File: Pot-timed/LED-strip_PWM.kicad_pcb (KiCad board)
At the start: 2 copper layers, 29.7 x 10 mm, 16 parts, among them IC1 MADW__ATTINY13-MM, P1 CONN_2, P2 CONN_2, T1 AO3400, U1 MCP1804-SOT23-5

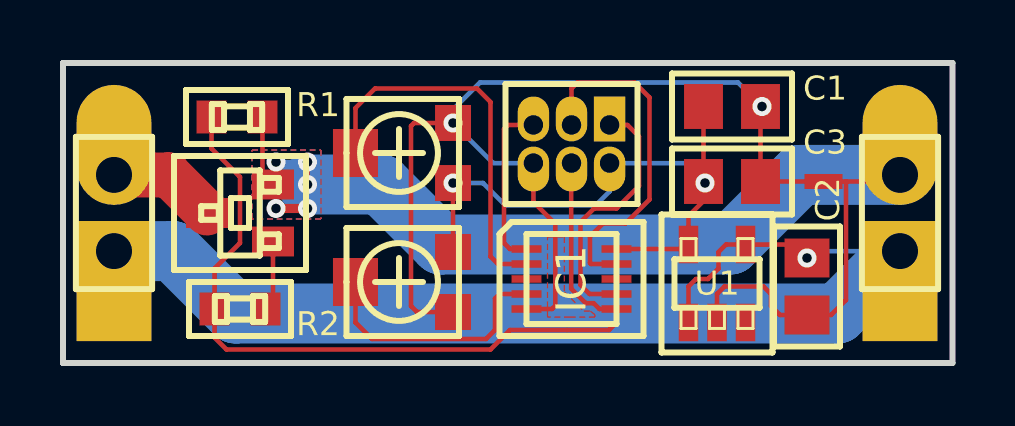
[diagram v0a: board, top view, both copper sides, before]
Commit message: Pot-timed (single board): rounded corners.
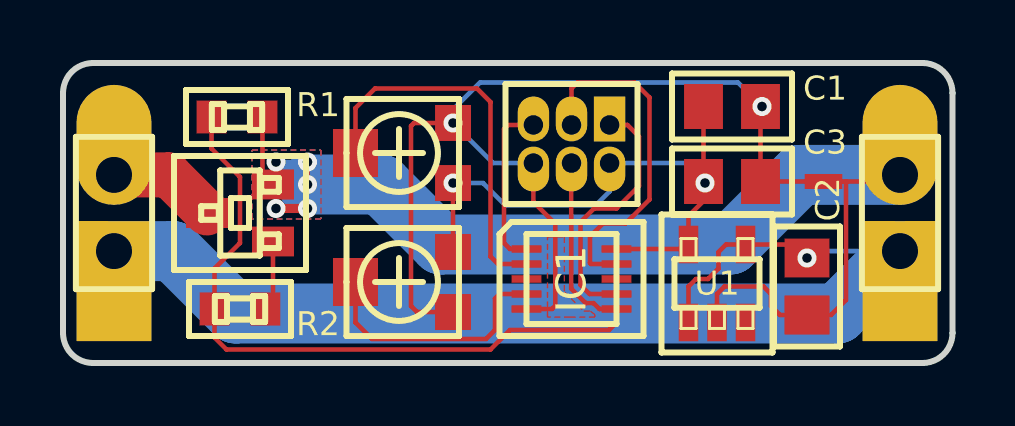
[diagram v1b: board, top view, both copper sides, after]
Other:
- outline, holes or cut-outs redrawn
- board text added: "V0.12 POT PWM controller"
- board text removed: "V0.11 POT PWM controller"
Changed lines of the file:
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@@
-(kicad_pcb (version 3) (host pcbnew "(2013-06-07 BZR 4197)-testing")
+(kicad_pcb (version 3) (host pcbnew "(2013-06-11 BZR 4208)-testing")
   (general
     (links 31)
     (no_connects 0)
-    (area 75.899999 47.899999 105.750001 58.100001)
+    (area 74.5076 46.6476 111.616669 61.100001)
     (thickness 1.6002)
-    (drawings 14)
+    (drawings 18)
     (tracks 156)
     (zones 0)
@@
     (title LED-strip_PWM)
     (date "24 May 2013")
-    (rev 0.11)
+    (rev 0.12)
     (company "2012 - blog.spitzenpfeil.org")
   )
@@
       (xy -0.90932 1.3462)) (layer B.SilkS) (width 0.00254))
   )
+  (gr_line (start 76 57) (end 76 49) (angle 90) (layer Edge.Cuts) (width 0.2))
+  (gr_line (start 104.65 58) (end 77 58) (angle 90) (layer Edge.Cuts) (width 0.2))
+  (gr_line (start 105.65 49) (end 105.65 57) (angle 90) (layer Edge.Cuts) (width 0.2))
+  (gr_line (start 77 48) (end 104.65 48) (angle 90) (layer Edge.Cuts) (width 0.2))
+  (gr_arc (start 104.65 49) (end 104.65 48) (angle 90) (layer Edge.Cuts) (width 0.2))
+  (gr_arc (start 104.65 57) (end 105.65 57) (angle 90) (layer Edge.Cuts) (width 0.2))
+  (gr_arc (start 77 57) (end 77 58) (angle 90) (layer Edge.Cuts) (width 0.2))
+  (gr_arc (start 77 49) (end 76 49) (angle 90) (layer Edge.Cuts) (width 0.2))
   (gr_text + (at 79.7 55.25 90) (layer B.SilkS)
     (effects (font (size 1 1) (thickness 0.2)) (justify mirror))
@@
     (arrow2b (pts (xy 76 59.3) (xy 77.126504 58.713579)))
   )
-  (gr_line (start 105.65 58) (end 76 58) (angle 90) (layer Edge.Cuts) (width 0.2))
-  (gr_line (start 76 48) (end 105.65 48) (angle 90) (layer Edge.Cuts) (width 0.2))
-  (gr_line (start 105.65 58) (end 105.65 48) (angle 90) (layer Edge.Cuts) (width 0.2))
-  (gr_line (start 76 48) (end 76 58) (angle 90) (layer Edge.Cuts) (width 0.2))
-  (gr_text "V0.11\nPOT PWM controller" (at 91 53.2) (layer B.SilkS)
+  (gr_text "V0.12\nPOT PWM controller" (at 91 53.2) (layer B.SilkS)
     (effects (font (size 1 1) (thickness 0.2032)) (justify mirror))
   )
@@
   (segment (start 93.15 48.65) (end 95.05 48.65) (width 0.1524) (layer Front) (net 6))
   (segment (start 92.95 48.85) (end 93.15 48.65) (width 0.1524) (layer Front) (net 6))
+  (segment (start 79.67 54.27) (end 81.75 56.35) (width 2) (layer Back) (net 7))
+  (segment (start 77.7 54.27) (end 79.67 54.27) (width 2) (layer Back) (net 7) (status 10))
+  (segment (start 103.9 54.27) (end 101.82 56.35) (width 2) (layer Back) (net 7) (status 20))
+  (segment (start 81.75 56.35) (end 101.82 56.35) (width 2) (layer Back) (net 7))
   (segment (start 96.85004 56.64794) (end 96.85004 55.44996) (width 0.1524) (layer Front) (net 7) (status 10))
   (segment (start 96.85004 55.44996) (end 97.1 55.2) (width 0.1524) (layer Front) (net 7))
@@
   (segment (start 97.85 54.3) (end 98.1 54.05) (width 0.1524) (layer Front) (net 7))
   (segment (start 98.1 54.05) (end 98.75 54.05) (width 0.1524) (layer Front) (net 7) (status 20))
-  (segment (start 77.7 54.27) (end 79.67 54.27) (width 2) (layer Back) (net 7) (status 10))
-  (segment (start 101.82 56.35) (end 103.9 54.27) (width 2) (layer Back) (net 7) (status 20))
-  (segment (start 81.75 56.35) (end 101.82 56.35) (width 2) (layer Back) (net 7))
-  (segment (start 79.67 54.27) (end 81.75 56.35) (width 2) (layer Back) (net 7))
   (via (at 100.8 54.50004) (size 0.635) (layers Front Back) (net 7) (status 30))
   (segment (start 100.8 54.50004) (end 101.03004 54.27) (width 0.1524) (layer Back) (net 7))

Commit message: Pot-timed (single board): switched to ATtiny10 SOT23-6.
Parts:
- IC1: value MADW__ATTINY13-MM -> ATTINY10-TS; footprint MADW__MLF10 -> MADW__SOT23-6
- JP1: value ISP -> TPI
- moved IC1 0.07 mm to (93.0, 55.2), turned to 90 degrees
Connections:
- IC1 pad 1: /RESET -> /GATE
- IC1 pad 2: /POT1 -> GND
- IC1 pad 3: N-000005 -> /POT1
- IC1 pad 5: GND -> VCC
- IC1 pad 6: /MOSI -> /RESET
- JP1 pad 1: /MISO -> /GATE
- JP1 pad 3: /SCK -> /POT1
- R1 pad 2: /MOSI -> /GATE
- R2 pad 1: /MOSI -> /GATE
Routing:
- net /GATE: track 0.00 -> 31.7 mm
- net /MOSI: track 29.2 -> 0.00 mm
- net /SCK: track 11.8 -> 0.00 mm
- net /MISO: track 8.66 -> 0.00 mm
- net /POT2: track 8.51 -> 16.5 mm
- net /RESET: track 5.67 -> 9.42 mm
- net /POT1: track 12.9 -> 15.3 mm
- net GND: track 34.1 -> 35.1 mm
- net VCC: track 20.0 -> 20.6 mm
- removed copper zone on F.Cu, net GND
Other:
- board text added: "V0.13 POT PWM controller"
- board text removed: "V0.12 POT PWM controller"

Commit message: Revert "Pot-timed (single board): switched to ATtiny10 SOT23-6."
This reverts commit c61ef78eb5273ce0300997b1b0118eed30148325.

C + ATtiny10 not supported by avr-gcc
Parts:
- IC1: value ATTINY10-TS -> MADW__ATTINY13-MM; footprint MADW__SOT23-6 -> MADW__MLF10
- JP1: value TPI -> ISP
- moved IC1 0.07 mm to (93.0, 55.2), turned to 0 degrees
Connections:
- IC1 pad 1: /GATE -> /RESET
- IC1 pad 2: GND -> /POT1
- IC1 pad 3: /POT1 -> N-000005
- IC1 pad 5: VCC -> GND
- IC1 pad 6: /RESET -> /MOSI
- JP1 pad 1: /GATE -> /MISO
- JP1 pad 3: /POT1 -> /SCK
- R1 pad 2: /GATE -> /MOSI
- R2 pad 1: /GATE -> /MOSI
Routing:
- net /GATE: track 31.7 -> 0.00 mm
- net /MOSI: track 0.00 -> 29.2 mm
- net /SCK: track 0.00 -> 11.8 mm
- net /MISO: track 0.00 -> 8.66 mm
- net /POT2: track 16.5 -> 8.51 mm
- net /RESET: track 9.42 -> 5.67 mm
- net /POT1: track 15.3 -> 12.9 mm
- net GND: track 35.1 -> 34.1 mm
- net VCC: track 20.6 -> 20.0 mm
- added copper zone on F.Cu, net GND
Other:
- board text added: "V0.12 POT PWM controller"
- board text removed: "V0.13 POT PWM controller"
